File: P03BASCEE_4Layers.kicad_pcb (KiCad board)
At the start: 2 copper layers, 39.6 x 37.6 mm, 21 parts, among them J1 Serial, J2 Digital, J3 ICSP, J4 I2C, U1 24LC1025, U2 24LC1025, U3 DS13375+, U4 ATMEGA328P-AU, Y1 Crystal 32MHz, Y2 Crystal 16MHz

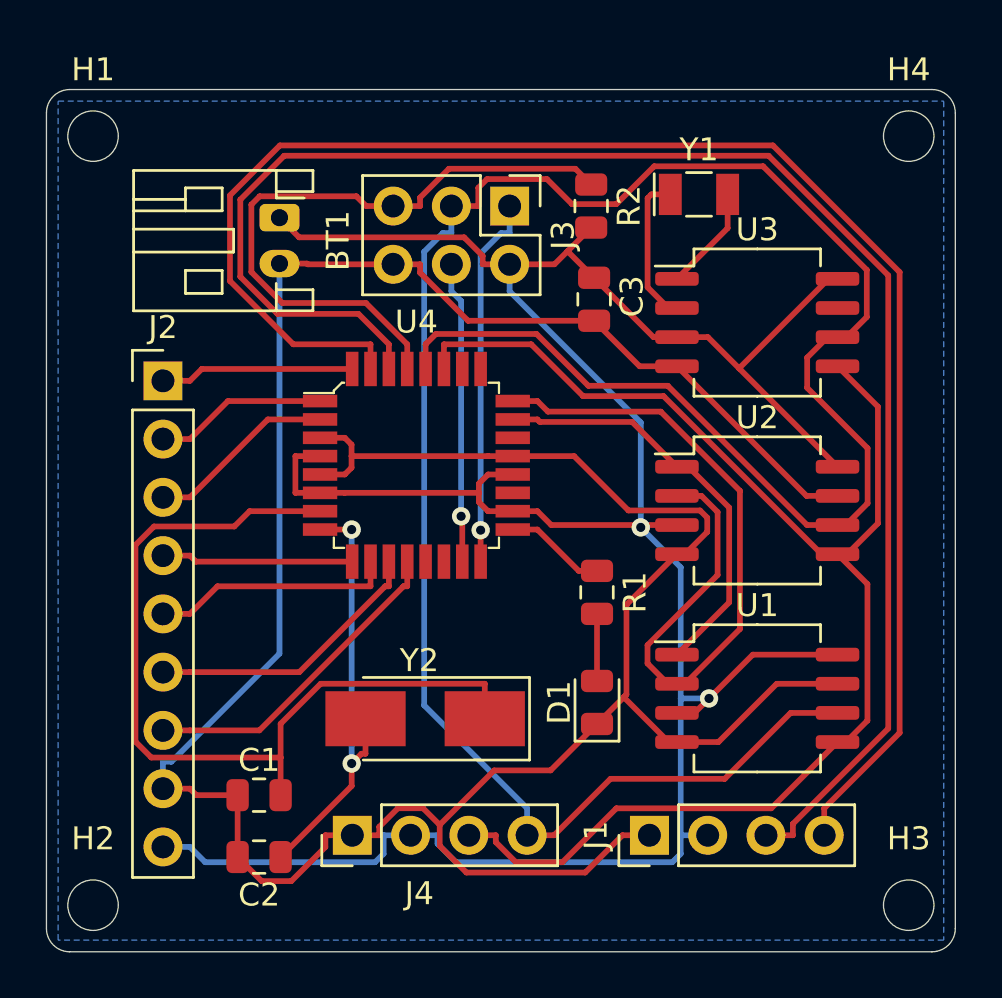
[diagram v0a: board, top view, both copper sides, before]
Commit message: Roteamento para quatro camadas, projeto principal com duas
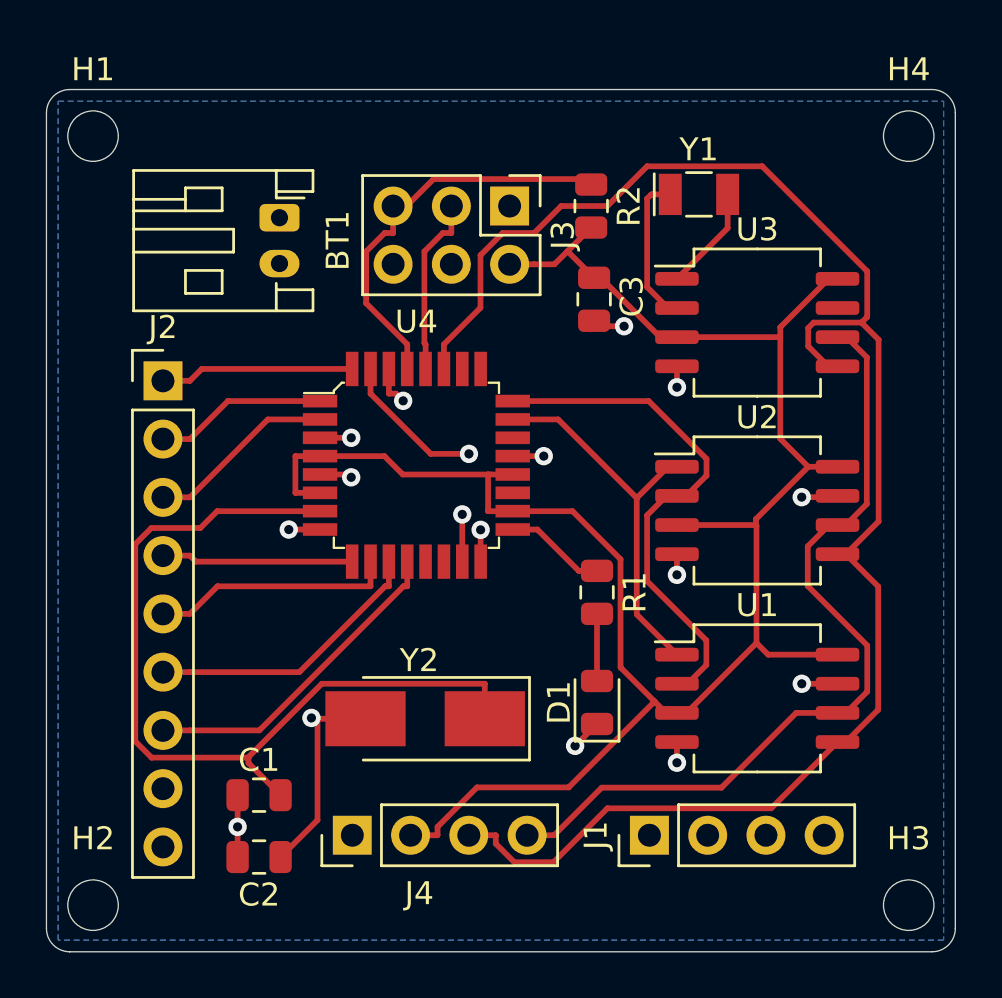
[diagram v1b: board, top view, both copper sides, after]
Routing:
- net GND: track 134.3 -> 15.4 mm, vias 0 -> 11
- net /RX: track 70.6 -> 27.3 mm, vias 0 -> 1
- net /TX: track 70.4 -> 29.6 mm, vias 0 -> 1
- net /SCK: track 105.0 -> 74.1 mm
- net /SDA: track 60.3 -> 73.2 mm
- net /RESET: track 28.4 -> 18.0 mm
- net /ADSS2: track 32.9 -> 22.7 mm
- net /VCC: track 123.1 -> 126.6 mm, vias 2 -> 0
- net /ADSS1: track 18.4 -> 16.7 mm
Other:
- copper layers 2 -> 4
